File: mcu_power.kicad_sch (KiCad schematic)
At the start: 36 parts, among them J1 830107834801, U1 MIMXRT1052CVJ5B, Y1 DSC1001BI5-024.0000

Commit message: finished v1
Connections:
- net DCDC_OUT: now also U1.F6 (VDD_SOC_IN), U1.F7 (VDD_SOC_IN), U1.F8 (VDD_SOC_IN), U1.F9 (VDD_SOC_IN), U1.G6 (VDD_SOC_IN), U1.G9 (VDD_SOC_IN), U1.H6 (VDD_SOC_IN), U1.H9 (VDD_SOC_IN)
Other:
- company: (none) -> Northeastern University
- title: (none) -> RT1050 DevBoard for Project Horizon
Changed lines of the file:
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@@
 	(generator_version "8.0")
 	(paper "A3")
+	(title_block
+		(title "RT1050 DevBoard for Project Horizon")
+		(rev "v1")
+		(company "Northeastern University")
+		(comment 1 "Built by Madhav Kapa")
+	)
 	(junction
 		(at 384.81 52.07)
@@
 	)
 	(junction
+		(at 189.23 43.18)
+		(diameter 0)
+		(color 0 0 0 0)
+	)
+	(junction
 		(at 215.9 35.56)
 		(diameter 0)
@@
 	)
 	(junction
+		(at 189.23 40.64)
+		(diameter 0)
+		(color 0 0 0 0)
+	)
+	(junction
 		(at 193.04 35.56)
 		(diameter 0)
@@
 	)
 	(junction
+		(at 189.23 38.1)
+		(diameter 0)
+		(color 0 0 0 0)
+	)
+	(junction
 		(at 384.81 69.85)
 		(diameter 0)
@@
 	)
 	(junction
+		(at 189.23 50.8)
+		(diameter 0)
+		(color 0 0 0 0)
+	)
+	(junction
 		(at 130.81 83.82)
 		(diameter 0)
@@
 	)
 	(junction
+		(at 189.23 45.72)
+		(diameter 0)
+		(color 0 0 0 0)
+	)
+	(junction
 		(at 384.81 67.31)
 		(diameter 0)
@@
 	)
 	(junction
+		(at 189.23 53.34)
+		(diameter 0)
+		(color 0 0 0 0)
+	)
+	(junction
 		(at 273.05 40.64)
 		(diameter 0)
@@
 	(junction
 		(at 238.76 35.56)
+		(diameter 0)
+		(color 0 0 0 0)
+	)
+	(junction
+		(at 189.23 48.26)
 		(diameter 0)
 		(color 0 0 0 0)
@@
 	(wire
 		(pts
+			(xy 189.23 53.34) (xy 189.23 55.88)
+		)
+		(stroke
+			(width 0)
+			(type default)
+		)
+	)
+	(wire
+		(pts
 			(xy 220.98 73.66) (xy 214.63 73.66)
 		)
@@
 	(wire
 		(pts
+			(xy 189.23 45.72) (xy 189.23 48.26)
+		)
+		(stroke
+			(width 0)
+			(type default)
+		)
+	)
+	(wire
+		(pts
 			(xy 138.43 154.94) (xy 143.51 154.94)
 		)
@@
 	(wire
 		(pts
+			(xy 189.23 40.64) (xy 189.23 43.18)
+		)
+		(stroke
+			(width 0)
+			(type default)
+		)
+	)
+	(wire
+		(pts
 			(xy 189.23 35.56) (xy 193.04 35.56)
 		)
@@
 	(wire
 		(pts
+			(xy 189.23 48.26) (xy 189.23 50.8)
+		)
+		(stroke
+			(width 0)
+			(type default)
+		)
+	)
+	(wire
+		(pts
 			(xy 58.42 44.45) (xy 46.99 44.45)
 		)
@@
 	(wire
 		(pts
+			(xy 189.23 43.18) (xy 189.23 45.72)
+		)
+		(stroke
+			(width 0)
+			(type default)
+		)
+	)
+	(wire
+		(pts
 			(xy 57.15 66.04) (xy 74.93 66.04)
 		)
@@
 	(wire
 		(pts
-			(xy 187.96 35.56) (xy 189.23 35.56)
-		)
-		(stroke
-			(width 0)
-			(type default)
-		)
-	)
-	(wire
-		(pts
 			(xy 149.86 148.59) (xy 160.02 148.59)
 		)
@@
 	(wire
 		(pts
+			(xy 189.23 50.8) (xy 189.23 53.34)
+		)
+		(stroke
+			(width 0)
+			(type default)
+		)
+	)
+	(wire
+		(pts
 			(xy 384.81 59.69) (xy 384.81 62.23)
 		)
@@
 	(wire
 		(pts
+			(xy 189.23 38.1) (xy 189.23 40.64)
+		)
+		(stroke
+			(width 0)
+			(type default)
+		)
+	)
+	(wire
+		(pts
 			(xy 27.94 38.1) (xy 39.37 38.1)
 		)
@@
 	(wire
 		(pts
-			(xy 187.96 35.56) (xy 187.96 55.88)
-		)
-		(stroke
+			(xy 189.23 35.56) (xy 189.23 38.1)
+		)
+		(stroke

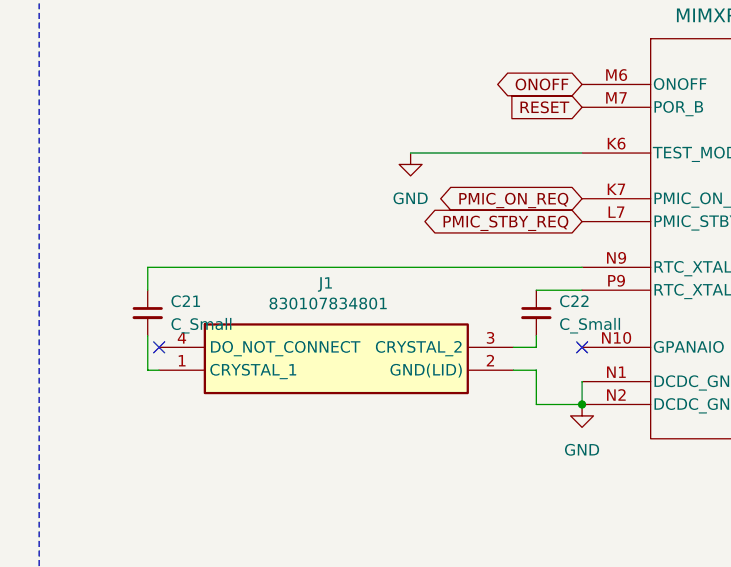
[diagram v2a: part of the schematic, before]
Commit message: added load switches
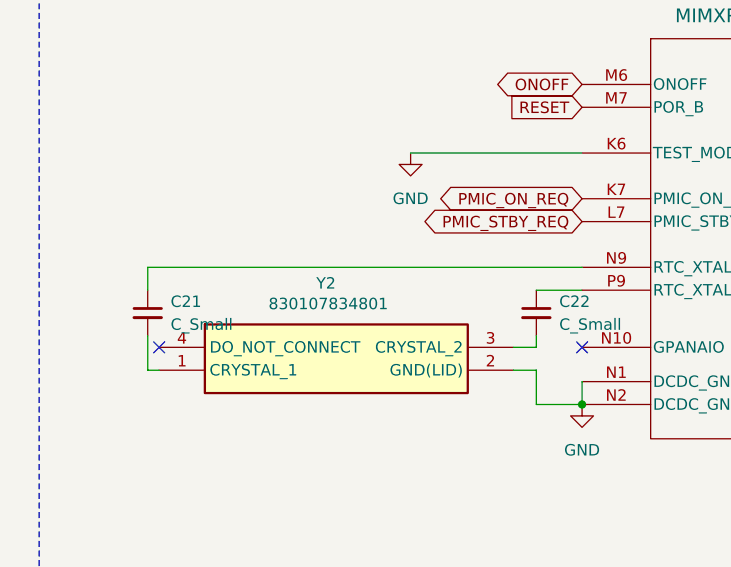
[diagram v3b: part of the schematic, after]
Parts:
- C1, C10, C11, C12, C13, C14, C15, C16, C17, C18, C19, C2, C20, C21, C22, C23, C24, C25, C26, C27, C28, C29, C3, C30, C31, C4, C5, C6, C7, C8, C9: footprint (none) -> Capacitor_SMD:C_0402_1005Metric
- L1: footprint (none) -> Inductor_SMD:L_0402_1005Metric
- R1: footprint (none) -> Resistor_SMD:R_0402_1005Metric
- renumbered J1 to Y2
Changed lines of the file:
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@@
 			)
 		)
-		(property "Footprint" ""
+		(property "Footprint" "Capacitor_SMD:C_0402_1005Metric"
 			(at 29.21 139.7 0)
 			(effects
@@
 			)
 		)
-		(property "Footprint" ""
+		(property "Footprint" "Capacitor_SMD:C_0402_1005Metric"
 			(at 123.19 107.95 0)
 			(effects
@@
 			)
 		)
-		(property "Footprint" ""
+		(property "Footprint" "Capacitor_SMD:C_0402_1005Metric"
 			(at 171.45 146.05 0)
 			(effects
@@
 			)
 		)
-		(property "Footprint" ""
+		(property "Footprint" "Resistor_SMD:R_0402_1005Metric"
 			(at 135.89 154.94 0)
 			(effects
@@
 			)
 		)
-		(property "Footprint" ""
+		(property "Footprint" "Capacitor_SMD:C_0402_1005Metric"
 			(at 261.62 38.1 0)
 			(effects
@@
 			)
 		)
-		(property "Footprint" ""
+		(property "Footprint" "Capacitor_SMD:C_0402_1005Metric"
 			(at 181.61 132.08 0)
 			(effects
@@
 			)
 		)
-		(property "Footprint" ""
+		(property "Footprint" "Capacitor_SMD:C_0402_1005Metric"
 			(at 72.39 139.7 0)
 			(effects
@@
 			)
 		)
-		(property "Footprint" ""
+		(property "Footprint" "Capacitor_SMD:C_0402_1005Metric"
 			(at 182.88 146.05 0)
 			(effects
@@
 			)
 		)
-		(property "Footprint" ""
+		(property "Footprint" "Capacitor_SMD:C_0402_1005Metric"
 			(at 46.99 46.99 0)
 			(effects
@@
 			)
 		)
-		(property "Footprint" ""
+		(property "Footprint" "Capacitor_SMD:C_0402_1005Metric"
 			(at 284.48 38.1 0)
 			(effects
@@
 			)
 		)
-		(property "Footprint" ""
+		(property "Footprint" "Capacitor_SMD:C_0402_1005Metric"
 			(at 100.33 77.47 0)
 			(effects
@@
 			)
 		)
-		(property "Footprint" ""
+		(property "Footprint" "Capacitor_SMD:C_0402_1005Metric"
 			(at 295.91 38.1 0)
 			(effects
@@
 			)
 		)
-		(property "Footprint" ""
+		(property "Footprint" "Capacitor_SMD:C_0402_1005Metric"
 			(at 273.05 38.1 0)
 			(effects
@@
 			)
 		)
-		(property "Footprint" ""
+		(property "Footprint" "Capacitor_SMD:C_0402_1005Metric"
 			(at 193.04 132.08 0)
 			(effects
@@
 			)
 		)
-		(property "Footprint" ""
+		(property "Footprint" "Capacitor_SMD:C_0402_1005Metric"
 			(at 238.76 38.1 0)
 			(effects
@@
 			)
 		)
-		(property "Footprint" ""
+		(property "Footprint" "Capacitor_SMD:C_0402_1005Metric"
 			(at 149.86 146.05 0)
 			(effects
@@
 			)
 		)
-		(property "Footprint" ""
+		(property "Footprint" "Capacitor_SMD:C_0402_1005Metric"
 			(at 204.47 38.1 0)
 			(effects
@@
 			)
 		)
-		(property "Footprint" ""
+		(property "Footprint" "Capacitor_SMD:C_0402_1005Metric"
 			(at 160.02 146.05 0)
 			(effects
@@
 			)
 		)
-		(property "Footprint" ""
+		(property "Footprint" "Capacitor_SMD:C_0402_1005Metric"
 			(at 74.93 68.58 0)
 			(effects
@@
 			)
 		)
-		(property "Footprint" ""
+		(property "Footprint" "Capacitor_SMD:C_0402_1005Metric"
 			(at 39.37 35.56 0)
 			(effects
@@
 			)
 		)
-		(property "Footprint" ""
+		(property "Footprint" "Capacitor_SMD:C_0402_1005Metric"
 			(at 215.9 38.1 0)
 			(effects
@@
 			)
 		)
-		(property "Footprint" ""
+		(property "Footprint" "Capacitor_SMD:C_0402_1005Metric"
 			(at 27.94 35.56 0)
 			(effects
@@
 			)
 		)
-		(property "Footprint" ""
+		(property "Footprint" "Capacitor_SMD:C_0402_1005Metric"
 			(at 137.16 146.05 0)
 			(effects
@@
 			)
 		)
-		(property "Footprint" ""
+		(property "Footprint" "Capacitor_SMD:C_0402_1005Metric"
 			(at 63.5 58.42 0)
 			(effects
@@
 			)
 		)
-		(property "Footprint" ""
+		(property "Footprint" "Capacitor_SMD:C_0402_1005Metric"
 			(at 250.19 38.1 0)
 			(effects
@@
 			)
 		)
-		(property "Footprint" ""
+		(property "Footprint" "Capacitor_SMD:C_0402_1005Metric"
 			(at 193.04 38.1 0)
 			(effects
@@
 			)
 		)
-		(property "Footprint" ""
+		(property "Footprint" "Capacitor_SMD:C_0402_1005Metric"
 			(at 58.42 46.99 0)
 			(effects
@@
 		(on_board yes)
 		(dnp no)
-		(property "Reference" "J1"
+		(property "Reference" "Y2"
 			(at 49.022 136.398 0)
 			(effects
@@
 			(project ""
 				(path "/dd9d031d-43a1-4442-b493-27451a14e0d9/ef9a9590-bc2d-4a19-b722-cc119a748157"
-					(reference "J1")
+					(reference "Y2")
 					(unit 1)
 				)
@@
 			)
 		)
-		(property "Footprint" ""
+		(property "Footprint" "Inductor_SMD:L_0402_1005Metric"
 			(at 173.99 129.54 0)
 			(effects
@@
 			)
 		)
-		(property "Footprint" ""
+		(property "Footprint" "Capacitor_SMD:C_0402_1005Metric"
 			(at 86.36 68.58 0)
 			(effects
@@
 			)
 		)
-		(property "Footprint" ""
+		(property "Footprint" "Capacitor_SMD:C_0402_1005Metric"
 			(at 227.33 38.1 0)
 			(effects
@@
 			)
 		)
-		(property "Footprint" ""
+		(property "Footprint" "Capacitor_SMD:C_0402_1005Metric"
 			(at 119.38 86.36 0)
 			(effects
@@
 			)
 		)
-		(property "Footprint" ""
+		(property "Footprint" "Capacitor_SMD:C_0402_1005Metric"
 			(at 128.27 160.02 0)
 			(effects
@@
 			)
 		)
-		(property "Footprint" ""
+		(property "Footprint" "Capacitor_SMD:C_0402_1005Metric"
 			(at 130.81 86.36 0)
 			(effects

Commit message: save before sdram redesign
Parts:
- C1, C10, C11, C12, C13, C14, C15, C16, C17, C18, C19, C2, C20, C23, C24, C25, C26, C27, C28, C3, C31, C4, C5, C6, C7, C8, C9: footprint Capacitor_SMD:C_0402_1005Metric -> Capacitor_SMD:C_0201_0603Metric
- C21, C22: value C_Small -> 8pF; footprint Capacitor_SMD:C_0402_1005Metric -> Capacitor_SMD:C_0201_0603Metric
- C29: value 0.22uH -> 0.22uF; footprint Capacitor_SMD:C_0402_1005Metric -> Capacitor_SMD:C_0201_0603Metric
- C30: value 33uH -> 33uF; footprint Capacitor_SMD:C_0402_1005Metric -> Capacitor_SMD:C_0805_2012Metric
- Y1: footprint DSC1001BI50240000 -> footprints:CDFN4_5X3P2_MCH
- Y2: footprint 830107834801 -> footprints:WE-XTAL_IQXC-146
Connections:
- net +3.3V: no longer C13.2, C14.2, C16.2, C17.2, C18.2, R1.2, U1.J5 (DCDC_SENSE), U1.M9 (VDD_SNVS_IN), U1.N14 (VDDA_ADC_3P3), U1.P12 (VDD_HIGH_IN)
- net DCDC_OUT: now also L1.1; no longer L1.2
- net GND: now also C21.2, C22.2
- net at U1.M1 (DCDC_LP), U1.M2 (DCDC_LP): now also L1.2; no longer L1.1
- net at C21.1, U1.N9 (RTC_XTALI): now also Y2.1 (CRYSTAL_1)
- net at C22.1, U1.P9 (RTC_XTALO): now also Y2.3 (CRYSTAL_2)
- new net DCDC_IN: C13.2, C14.2, C16.2, C17.2, C18.2, R1.2, U1.J5 (DCDC_SENSE), U1.M9 (VDD_SNVS_IN), U1.N14 (VDDA_ADC_3P3), U1.P12 (VDD_HIGH_IN)
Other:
- moved on the sheet: L1, Y2
